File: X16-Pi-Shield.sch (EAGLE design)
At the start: 50 parts, among them J3 CONN_DF13-4P-1.25DSA, J4 SAMTEC-HTST-110-04-X-D-RAJ, J5 BM04B-GHS-TBT, Q2 2.5A/30V/105mΩ, Q3 220mA/50V/3.5Ω, U1 INA260AIPW, U2 AZ1117IH-3.3TRG1, Y2 ECS-80-S-4X

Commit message: started labeling schematic
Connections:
- removed net PI_POWER: C14.+, JP3.1, JP4.1
- net 5V: now also C14.+, JP3.1, JP4.1; no longer JP3.2, JP4.2
- net 5V_EXT: now also JP3.2, JP4.2
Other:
- note added: "3v3 test point"
- note added: "5v test point"
- note added: "BNO055 IMU"
- note added: "FXOS8700-FXAS21002"
- note added: "GND test point"
- note added: "I2C Pull-up Resistors"
- note added: "I2C connector"
- note added: "IMU"
- note added: "Only pull ADR high if wanting to change address from 0x28 to 0x29; use 0Ohm to do so, as breakout board has a pull down resistor"
- note added: "Oscillator ECS-80-18-4X"
- note added: "SPI connector"
- note added: "UART connector"
- note added: "power jumpers"
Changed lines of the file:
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@@
 <sheet>
 <plain>
+<text x="33.02" y="30.48" size="1.778" layer="91">Oscillator
+ECS-80-18-4X</text>
+<text x="17.78" y="160.02" size="1.778" layer="91">IMU</text>
+<text x="2.54" y="157.48" size="1.778" layer="91">FXOS8700-FXAS21002</text>
+<text x="58.42" y="170.18" size="1.778" layer="91">3v3 test point</text>
+<text x="60.96" y="162.56" size="1.778" layer="91">5v test point</text>
+<text x="58.42" y="154.94" size="1.778" layer="91">GND test point</text>
+<text x="68.58" y="5.08" size="1.778" layer="91">I2C Pull-up Resistors</text>
+<text x="40.64" y="111.76" size="1.778" layer="91">BNO055 IMU</text>
+<text x="68.58" y="76.2" size="1.778" layer="91">Only pull ADR high if wanting
+to change address from
+0x28 to 0x29;
+use 0Ohm to do so, as breakout board
+has a pull down resistor</text>
+<text x="55.88" y="43.18" size="1.778" layer="91">I2C connector</text>
+<text x="114.3" y="33.02" size="1.778" layer="91">I2C connector</text>
+<text x="149.86" y="53.34" size="1.778" layer="91">I2C connector</text>
+<text x="231.14" y="45.72" size="1.778" layer="91">I2C connector</text>
+<text x="185.42" y="38.1" size="1.778" layer="91">UART connector</text>
+<text x="142.24" y="12.7" size="1.778" layer="91">power jumpers</text>
+<text x="83.82" y="58.42" size="1.778" layer="91">SPI connector</text>
 </plain>
 <instances>
@@
 </segment>
 </net>
-<net name="PI_POWER" class="0">
+<net name="5V" class="0">
+<segment>
+<pinref part="TP2" gate="G$1" pin="1"/>
+<label x="81.28" y="162.56" size="1.778" layer="95"/>
+<wire x1="83.82" y1="162.56" x2="73.66" y2="162.56" width="0.1524" layer="91"/>
+</segment>
+<segment>
+<pinref part="U$1" gate="G$1" pin="5V@2"/>
+<wire x1="114.3" y1="160.02" x2="114.3" y2="167.64" width="0.1524" layer="91"/>
+<label x="114.3" y="162.56" size="1.778" layer="95" rot="R90"/>
+</segment>
+<segment>
+<pinref part="U$1" gate="G$1" pin="5V@4"/>
+<wire x1="119.38" y1="160.02" x2="119.38" y2="167.64" width="0.1524" layer="91"/>
+<label x="116.84" y="165.1" size="1.778" layer="95" rot="R270"/>
+</segment>
 <segment>
 <wire x1="157.48" y1="20.32" x2="162.56" y2="20.32" width="0.1524" layer="91"/>
@@
 </segment>
 </net>
-<net name="5V" class="0">
-<segment>
-<wire x1="147.32" y1="30.48" x2="144.78" y2="30.48" width="0.1524" layer="91"/>
-<wire x1="144.78" y1="30.48" x2="144.78" y2="22.86" width="0.1524" layer="91"/>
-<wire x1="144.78" y1="22.86" x2="144.78" y2="20.32" width="0.1524" layer="91"/>
-<wire x1="144.78" y1="20.32" x2="147.32" y2="20.32" width="0.1524" layer="91"/>
-<wire x1="144.78" y1="22.86" x2="142.24" y2="22.86" width="0.1524" layer="91"/>
-<junction x="144.78" y="22.86"/>
-<pinref part="JP3" gate="G$1" pin="2"/>
-<pinref part="JP4" gate="G$1" pin="2"/>
-<label x="142.24" y="22.86" size="1.778" layer="95"/>
-</segment>
-<segment>
-<pinref part="TP2" gate="G$1" pin="1"/>
-<label x="81.28" y="162.56" size="1.778" layer="95"/>
-<wire x1="83.82" y1="162.56" x2="73.66" y2="162.56" width="0.1524" layer="91"/>
-</segment>
-<segment>
-<pinref part="U$1" gate="G$1" pin="5V@2"/>
-<wire x1="114.3" y1="160.02" x2="114.3" y2="167.64" width="0.1524" layer="91"/>
-<label x="114.3" y="162.56" size="1.778" layer="95" rot="R90"/>
-</segment>
-<segment>
-<pinref part="U$1" gate="G$1" pin="5V@4"/>
-<wire x1="119.38" y1="160.02" x2="119.38" y2="167.64" width="0.1524" layer="91"/>
-<label x="116.84" y="165.1" size="1.778" layer="95" rot="R270"/>
-</segment>
-</net>
 <net name="3VO_1" class="0">
 <segment>
@@
 </segment>
 </net>
+<net name="5V_EXT" class="0">
+<segment>
+<pinref part="JP4" gate="G$1" pin="2"/>
+<wire x1="147.32" y1="30.48" x2="147.32" y2="27.94" width="0.1524" layer="91"/>
+<wire x1="147.32" y1="27.94" x2="144.78" y2="27.94" width="0.1524" layer="91"/>
+<pinref part="JP3" gate="G$1" pin="2"/>
+<wire x1="147.32" y1="20.32" x2="147.32" y2="27.94" width="0.1524" layer="91"/>
+<junction x="147.32" y="27.94"/>
+<label x="142.24" y="27.94" size="1.778" layer="95"/>
+</segment>
+</net>

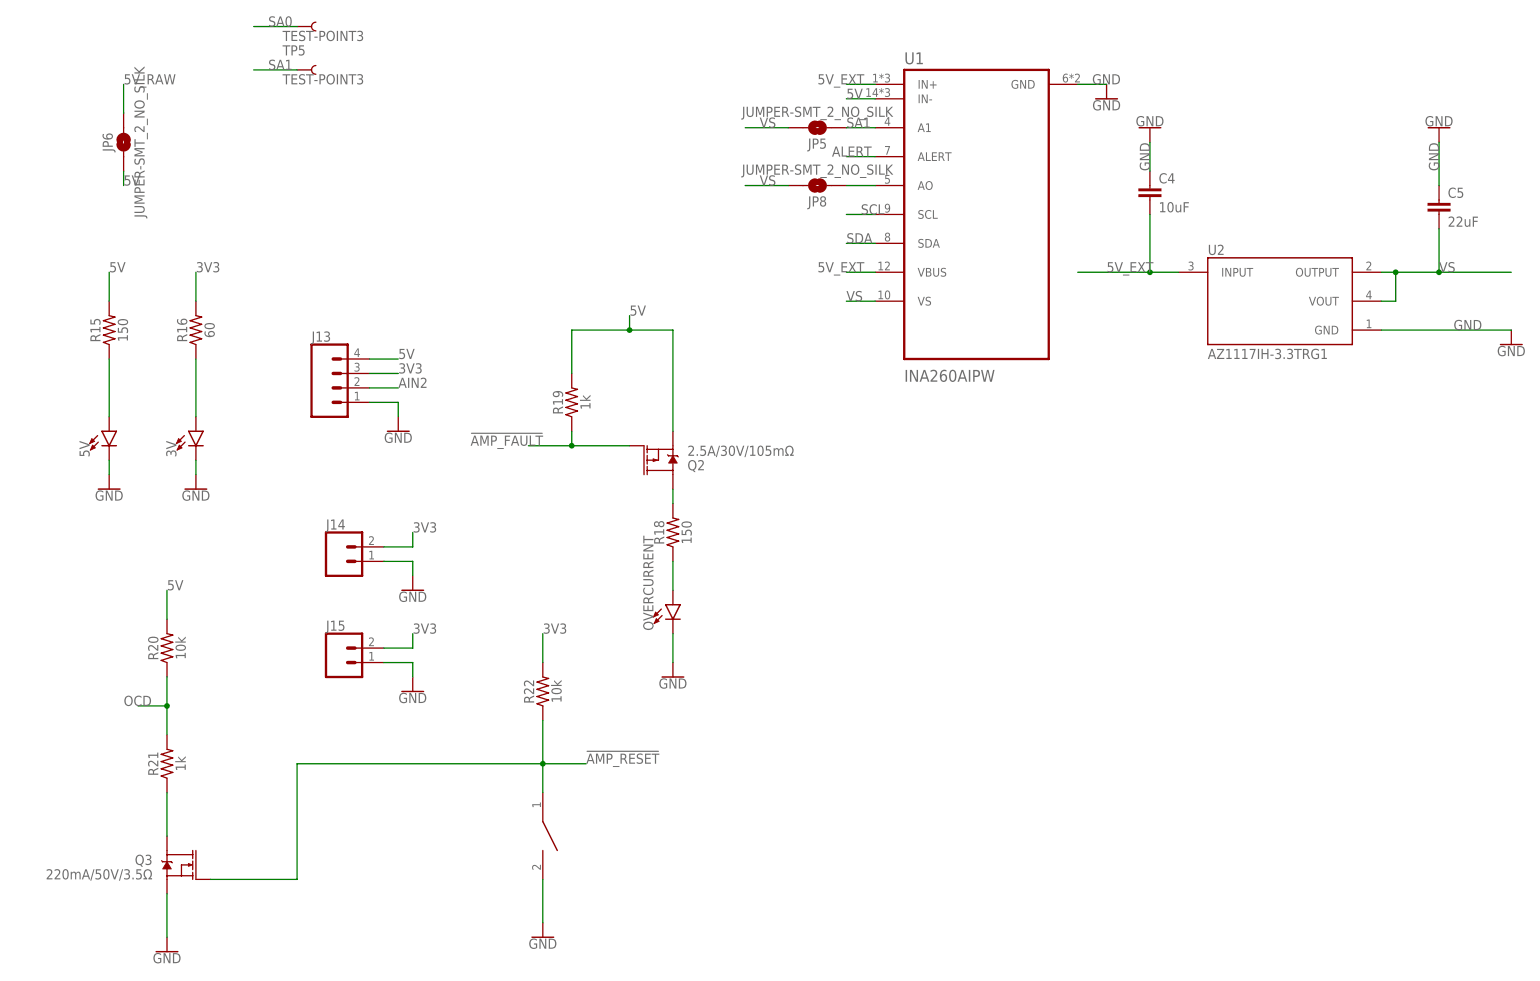
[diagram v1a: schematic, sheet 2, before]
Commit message: updated schematuc with labels
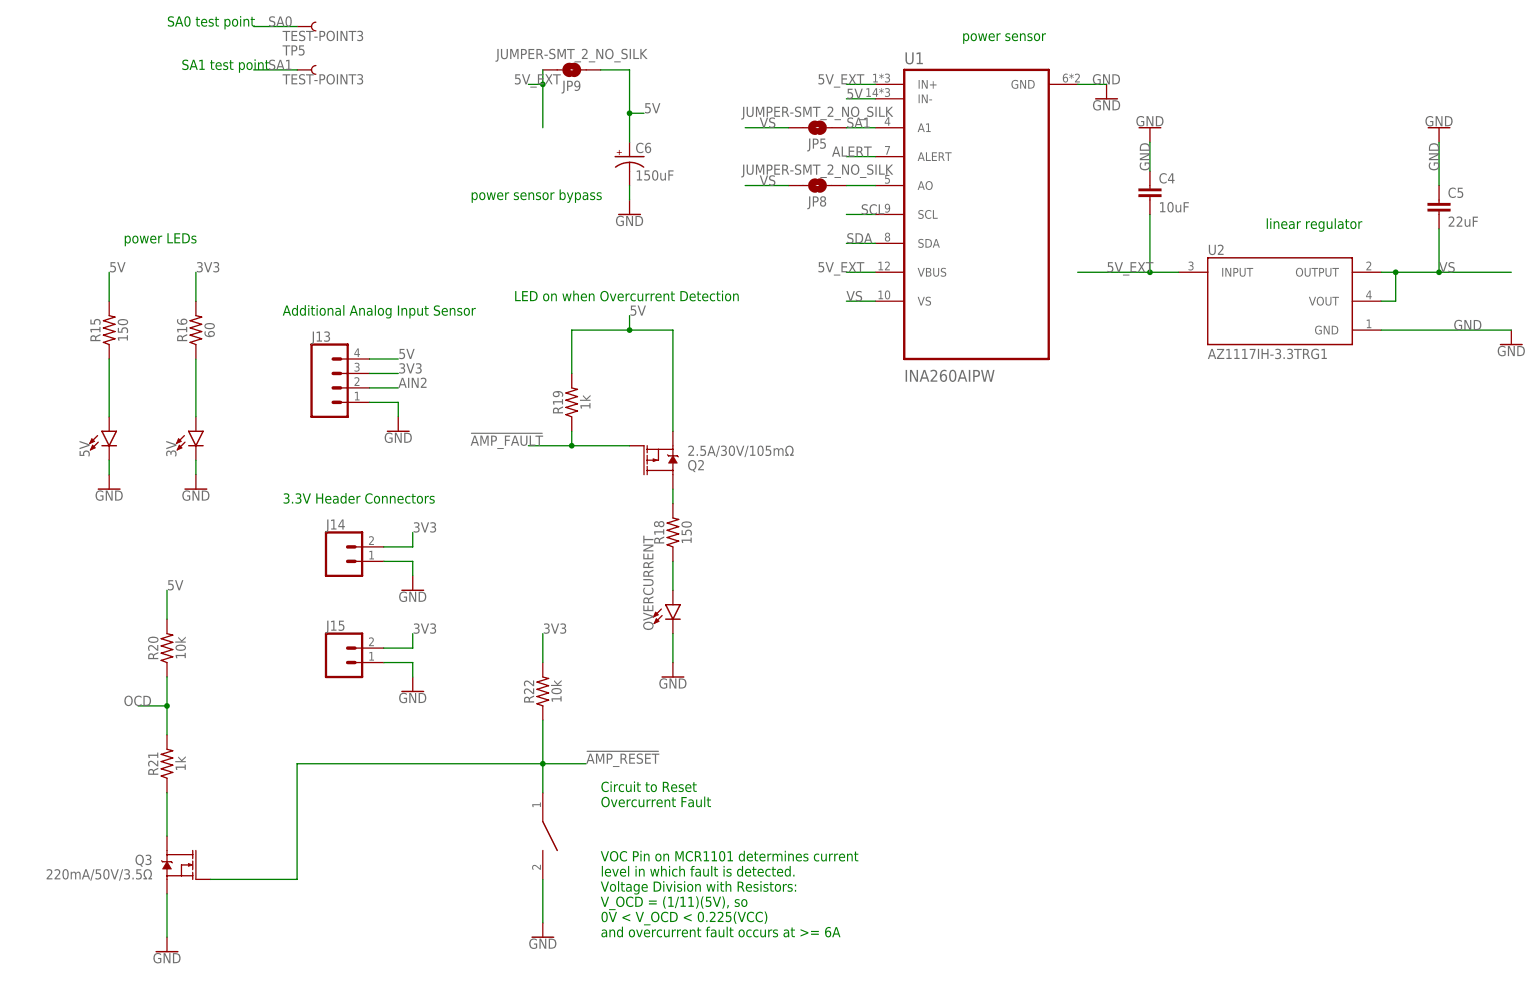
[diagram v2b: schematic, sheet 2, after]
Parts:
- removed JP6: JUMPER-SMT_2_NO_SILK, SparkFun-Jumpers:JUMPER-SMT_2_NO_SILK
- added C6: 150uF, X15-Pi-Shield-Parts:C-TANTALUM(10UF_150UF)
- added JP9: JUMPER-SMT_2_NO_SILK, SparkFun-Jumpers:JUMPER-SMT_2_NO_SILK
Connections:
- removed net 5V_RAW: JP6.2
- net 5V: now also C6.+, JP9.1; no longer JP6.1
- net 5V_EXT: now also JP9.2
- net GND: now also C6.-
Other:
- note added: "3.3V Header Connectors"
- note added: "Additional Analog Input Sensor"
- note added: "Circuit to Reset Overcurrent Fault"
- note added: "LED on when Overcurrent Detection"
- note added: "SA0 test point"
- note added: "SA1 test point"
- note added: "VOC Pin on MCR1101 determines current level in which fault is detected. Voltage Division with Resistors: V_OCD = (1/11)(5V), so 0V < V_OCD < 0.225(VCC) and overcurrent fault occurs at >= 6A"
- note added: "connecor to backplane"
- note added: "linear regulator"
- note added: "power LEDs"
- note added: "power sensor"
- note added: "power sensor bypass"
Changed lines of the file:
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@@
 <part name="TP3" library="SparkFun-Connectors" deviceset="TEST-POINT" device="3"/>
 <part name="FRAME2" library="SparkFun-Aesthetics" deviceset="FRAME-A4L" device=""/>
-<part name="JP6" library="SparkFun-Jumpers" deviceset="JUMPER-SMT_2_NO" device="_SILK"/>
 <part name="5V" library="SparkFun-LED" deviceset="LED" device="0603"/>
 <part name="3V" library="SparkFun-LED" deviceset="LED" device="0603"/>
@@
 <part name="J5" library="X16-Pi-Shield" deviceset="BM04B-GHS-TBT" device=""/>
 <part name="GND20" library="supply1" library_urn="urn:adsk.eagle:library:371" deviceset="GND" device=""/>
+<part name="GND10" library="SparkFun-PowerSymbols" deviceset="GND" device=""/>
+<part name="C6" library="X15-Pi-Shield-Parts" deviceset="C-TANTALUM(10UF_150UF)" device="" value="150uF"/>
+<part name="JP9" library="SparkFun-Jumpers" deviceset="JUMPER-SMT_2_NO" device="_SILK"/>
 </parts>
 <sheets>
@@
 <sheet>
 <plain>
+<text x="25.4" y="172.72" size="1.778" layer="91">SA0 test point</text>
+<text x="27.94" y="165.1" size="1.778" layer="91">SA1 test point</text>
+<text x="17.78" y="134.62" size="1.778" layer="91">power LEDs</text>
+<text x="45.72" y="121.92" size="1.778" layer="91">Additional Analog Input Sensor</text>
+<text x="45.72" y="88.9" size="1.778" layer="91">3.3V Header Connectors</text>
+<text x="86.36" y="124.46" size="1.778" layer="91">LED on when Overcurrent Detection</text>
+<text x="101.6" y="35.56" size="1.778" layer="91">Circuit to Reset
+Overcurrent Fault</text>
+<text x="101.6" y="12.7" size="1.778" layer="91">VOC Pin on MCR1101 determines current
+level in which fault is detected.
+Voltage Division with Resistors:
+V_OCD = (1/11)(5V), so
+0V &lt; V_OCD &lt; 0.225(VCC)
+and overcurrent fault occurs at &gt;= 6A</text>
+<text x="165.1" y="170.18" size="1.778" layer="91">power sensor</text>
+<text x="218.44" y="137.16" size="1.778" layer="91">linear regulator</text>
+<text x="78.74" y="142.24" size="1.778" layer="91">power sensor bypass</text>
 </plain>
 <instances>
@@
 <attribute name="DESIGNER" x="226.26" y="6.35" size="2.54" layer="94" font="vector"/>
 </instance>
-<instance part="JP6" gate="G$1" x="17.78" y="152.4" smashed="yes" rot="R90">
-<attribute name="NAME" x="14.986" y="152.4" size="1.778" layer="95" font="vector" rot="R90" align="center"/>
-<attribute name="VALUE" x="20.574" y="152.4" size="1.778" layer="96" font="vector" rot="R90" align="center"/>
-</instance>
 <instance part="5V" gate="G$1" x="15.24" y="101.6" smashed="yes">
 <attribute name="NAME" x="11.811" y="97.028" size="1.778" layer="95" font="vector" rot="R90"/>
@@
 <attribute name="NAME" x="139.7" y="141.986" size="1.778" layer="95" font="vector" rot="R180" align="center"/>
 <attribute name="VALUE" x="139.7" y="147.574" size="1.778" layer="96" font="vector" rot="R180" align="center"/>
+</instance>
+<instance part="GND10" gate="1" x="106.68" y="139.7" smashed="yes">
+<attribute name="VALUE" x="106.68" y="139.446" size="1.778" layer="96" align="top-center"/>
+</instance>
+<instance part="C6" gate="G$1" x="106.68" y="149.86" smashed="yes">
+<attribute name="NAME" x="107.696" y="150.495" size="1.778" layer="95"/>
+<attribute name="VALUE" x="107.696" y="145.669" size="1.778" layer="96"/>
+</instance>
+<instance part="JP9" gate="G$1" x="96.52" y="165.1" smashed="yes" rot="R180">
+<attribute name="NAME" x="96.52" y="162.306" size="1.778" layer="95" font="vector" rot="R180" align="center"/>
+<attribute name="VALUE" x="96.52" y="167.894" size="1.778" layer="96" font="vector" rot="R180" align="center"/>
 </instance>
 </instances>
@@
 <nets>
 <net name="5V" class="0">
-<segment>
-<wire x1="17.78" y1="147.32" x2="17.78" y2="144.78" width="0.1524" layer="91"/>
-<label x="17.78" y="144.78" size="1.778" layer="95"/>
-<pinref part="JP6" gate="G$1" pin="1"/>
-</segment>
 <segment>
 <pinref part="R15" gate="G$1" pin="2"/>
@@
 <label x="144.78" y="160.02" size="1.778" layer="95"/>
 </segment>
-</net>
-<net name="5V_RAW" class="0">
-<segment>
-<wire x1="17.78" y1="157.48" x2="17.78" y2="162.56" width="0.1524" layer="91"/>
-<label x="17.78" y="162.56" size="1.778" layer="95"/>
-<pinref part="JP6" gate="G$1" pin="2"/>
+<segment>
+<wire x1="101.6" y1="165.1" x2="106.68" y2="165.1" width="0.1524" layer="91"/>
+<wire x1="106.68" y1="165.1" x2="106.68" y2="157.48" width="0.1524" layer="91"/>
+<wire x1="106.68" y1="157.48" x2="106.68" y2="152.4" width="0.1524" layer="91"/>
+<wire x1="106.68" y1="157.48" x2="109.22" y2="157.48" width="0.1524" layer="91"/>
+<junction x="106.68" y="157.48"/>
+<label x="109.22" y="157.48" size="1.778" layer="95"/>
+<pinref part="C6" gate="G$1" pin="+"/>
+<pinref part="JP9" gate="G$1" pin="1"/>
 </segment>
 </net>
@@
 <wire x1="248.92" y1="152.4" x2="248.92" y2="144.78" width="0.1524" layer="91"/>
 <label x="248.92" y="147.32" size="1.778" layer="95" rot="R90"/>
+</segment>
+<segment>
+<wire x1="106.68" y1="144.78" x2="106.68" y2="142.24" width="0.1524" layer="91"/>
+<pinref part="GND10" gate="1" pin="GND"/>
+<pinref part="C6" gate="G$1" pin="-"/>
 </segment>
 </net>
@@
 <junction x="198.12" y="129.54"/>
 <pinref part="C4" gate="G$1" pin="2"/>
+</segment>
+<segment>
+<pinref part="JP9" gate="G$1" pin="2"/>
+<wire x1="91.44" y1="165.1" x2="91.44" y2="162.56" width="0.1524" layer="91"/>
+<wire x1="91.44" y1="162.56" x2="88.9" y2="162.56" width="0.1524" layer="91"/>
+<wire x1="91.44" y1="154.94" x2="91.44" y2="162.56" width="0.1524" layer="91"/>
+<junction x="91.44" y="162.56"/>
+<label x="86.36" y="162.56" size="1.778" layer="95"/>
 </segment>
 </net>
@@
 <sheet>
 <plain>
+<text x="66.04" y="111.76" size="1.778" layer="91">connecor to backplane</text>
 </plain>
 <instances>

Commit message: removed unused components and added new imu
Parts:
- removed C14: 150uF, X15-Pi-Shield-Parts:C-TANTALUM(10UF_150UF)
- removed J13: (no value), SparkFun-Connectors:CONN_04
- removed JP1, JP2, JP3, JP4: JUMPER-SMT_2_NO_SILK, SparkFun-Jumpers:JUMPER-SMT_2_NO_SILK
- removed OVERCURRENT: (no value), SparkFun-LED:LED0603
- removed Q2: 2.5A/30V/105mΩ, SparkFun-DiscreteSemi:MOSFET_PCH-DMG2307L
- removed Q3: 220mA/50V/3.5Ω, SparkFun-DiscreteSemi:MOSFET-NCH-BSS138
- removed R18: 150, SparkFun-Resistors:RESISTOR0603
- removed R19, R21: 1k, SparkFun-Resistors:RESISTOR0603
- removed R20, R22: 10k, SparkFun-Resistors:RESISTOR0603
- removed TP1, TP2, TP3: TEST-POINT3, SparkFun-Connectors:TEST-POINT3
- removed U$4: CONN_ADAFRUIT-FXOS8700-FXAS21002, X16-Pi-Shield:CONN_ADAFRUIT-FXOS8700-FXAS21002
- removed U$7: (no value), X16-Pi-Shield:SWITCH_DISCRETECOMPONENTS
- removed Y2: ECS-80-S-4X, X15-Pi-Shield-Parts:ECS-80-S-4X
- added C7: 150uF, X15-Pi-Shield-Parts:C-TANTALUM(10UF_150UF)
- added C8: 0.1uF, SparkFun-Capacitors:0.1UF-0603-25V-(+80/-20%)
- added JP10, JP6: JUMPER-SMT_2_NO_SILK, SparkFun-Jumpers:JUMPER-SMT_2_NO_SILK
- added TP6, TP7, TP8: TEST-POINT3, SparkFun-Connectors:TEST-POINT3
- added U3: BNO080, X16-Pi-Shield:BNO080
- C1, C2: value 18pF -> 120uF; device SparkFun-Capacitors:18PF-0603-50V-5% -> SparkFun-Capacitors:10UF-POLAR-0603-6.3V-20%(TANT)
- J4: value SAMTEC-HTST-110-04-X-D-RAJ -> HTST-110-04-L-D-RA; device SAMTEC-HTST-110-04-X-D-RA:SAMTEC-HTST-110-04-X-D-RAJ -> X16-Pi-Shield:HTST-110-04-L-D-RA
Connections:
- net 3V0_2 renamed 3VO
- removed net !AMP_FAULT: Q2.G, R19.1
- removed net !AMP_RESET: Q3.G, R22.1, U$7.P$1
- removed net 3VO_1: U$4.3VO
- removed net AIN2: J13.2
- removed net AMP_RESET: U$1.GPIO4
- removed net A_INT: U$1.GPIO7, U$4.AI1
- removed net DGND: J4.9, U$1.GPIO6
- removed net GPIO1: J4.2
- removed net GPIO2: J4.4
- removed net GPIO3: J4.6
- removed net GPIO4: J4.8
- removed net INT: U$1.GPIO26
- removed net N$1: C1.1, JP1.1, Y2.1
- removed net N$12: Q2.D, R18.2
- removed net N$13: OVERCURRENT.A, R18.1
- removed net N$14: Q3.D, R21.1
- removed net N$16: U$1.ID_SC*
- removed net N$2: C2.1, JP2.1, Y2.2
- removed net N$29: U$1.ID_SD*
- removed net OCD: R20.1, R21.2
- removed net OSC1: JP2.2
- removed net OSC2: JP1.2
- removed net RX0_INT: U$1.GPIO19
- removed net RX1_INT: U$1.GPIO5
- removed net SCI: U$1.GPIO3
- new net GPIO_5: J4.9, U$1.GPIO7
- new net GPIO_6: J4.5, U$1.GPIO6
- new net GPIO_7: J4.10, U$1.GPIO5
- new net GPIO_8: J4.12, U$1.GPIO4
- net 3V3: now also C8.1, TP6.1, U3.VDD, U3.VDDIO; no longer J13.3, R22.2, TP1.1, U$4.VIN
- net 5V: now also C1.+, C2.+, C7.+, JP10.1, JP6.1, TP7.1; no longer C14.+, J13.4, JP3.1, JP4.1, Q2.S, R19.2, R20.2, TP2.1
- net 5V_EXT: now also JP10.2, JP6.2; no longer JP3.2, JP4.2
- net GND: now also C1.-, C2.-, C7.-, C8.2, TP8.1, U3.GND, U3.GNDIO; no longer C1.2, C14.-, C2.2, J13.1, OVERCURRENT.C, Q3.S, TP3.1, U$4.GND, U$7.P$2
- net GPIO_1: now also J4.2
- net GPIO_2: now also J4.4
- net GPIO_3: now also J4.6
- net GPIO_4: now also J4.8
- net IMU_INT: no longer U$4.GI1
- net IMU_RESET: no longer U$4.RST
- net SCL: now also U$1.GPIO3; no longer U$4.SCL
- net SDA: no longer U$4.SDA
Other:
- note removed: "Additional Analog Input Sensor"
- note removed: "Circuit to Reset Overcurrent Fault"
- note removed: "FXOS8700-FXAS21002"
- note removed: "IMU"
- note removed: "LED on when Overcurrent Detection"
- note removed: "Oscillator ECS-80-18-4X"
- note removed: "VOC Pin on MCR1101 determines current level in which fault is detected. Voltage Division with Resistors: V_OCD = (1/11)(5V), so 0V < V_OCD < 0.225(VCC) and overcurrent fault occurs at >= 6A"
